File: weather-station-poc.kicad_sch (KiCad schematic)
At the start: 14 parts

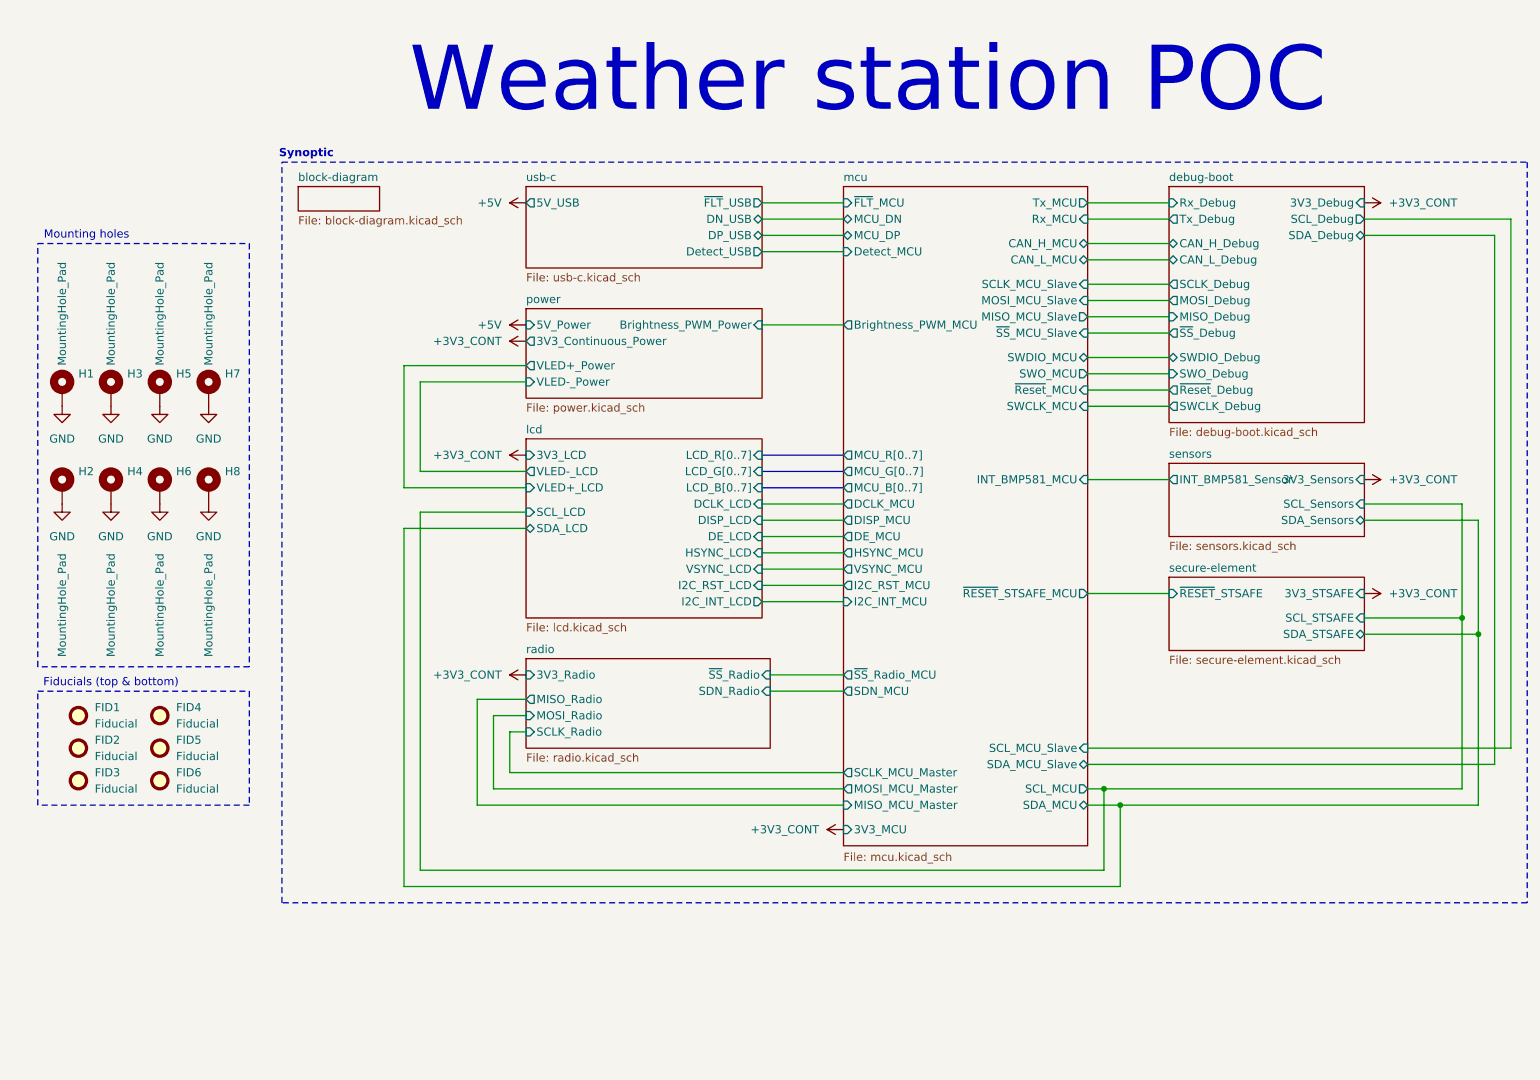
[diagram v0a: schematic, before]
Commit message: Rename main 3V3 label name
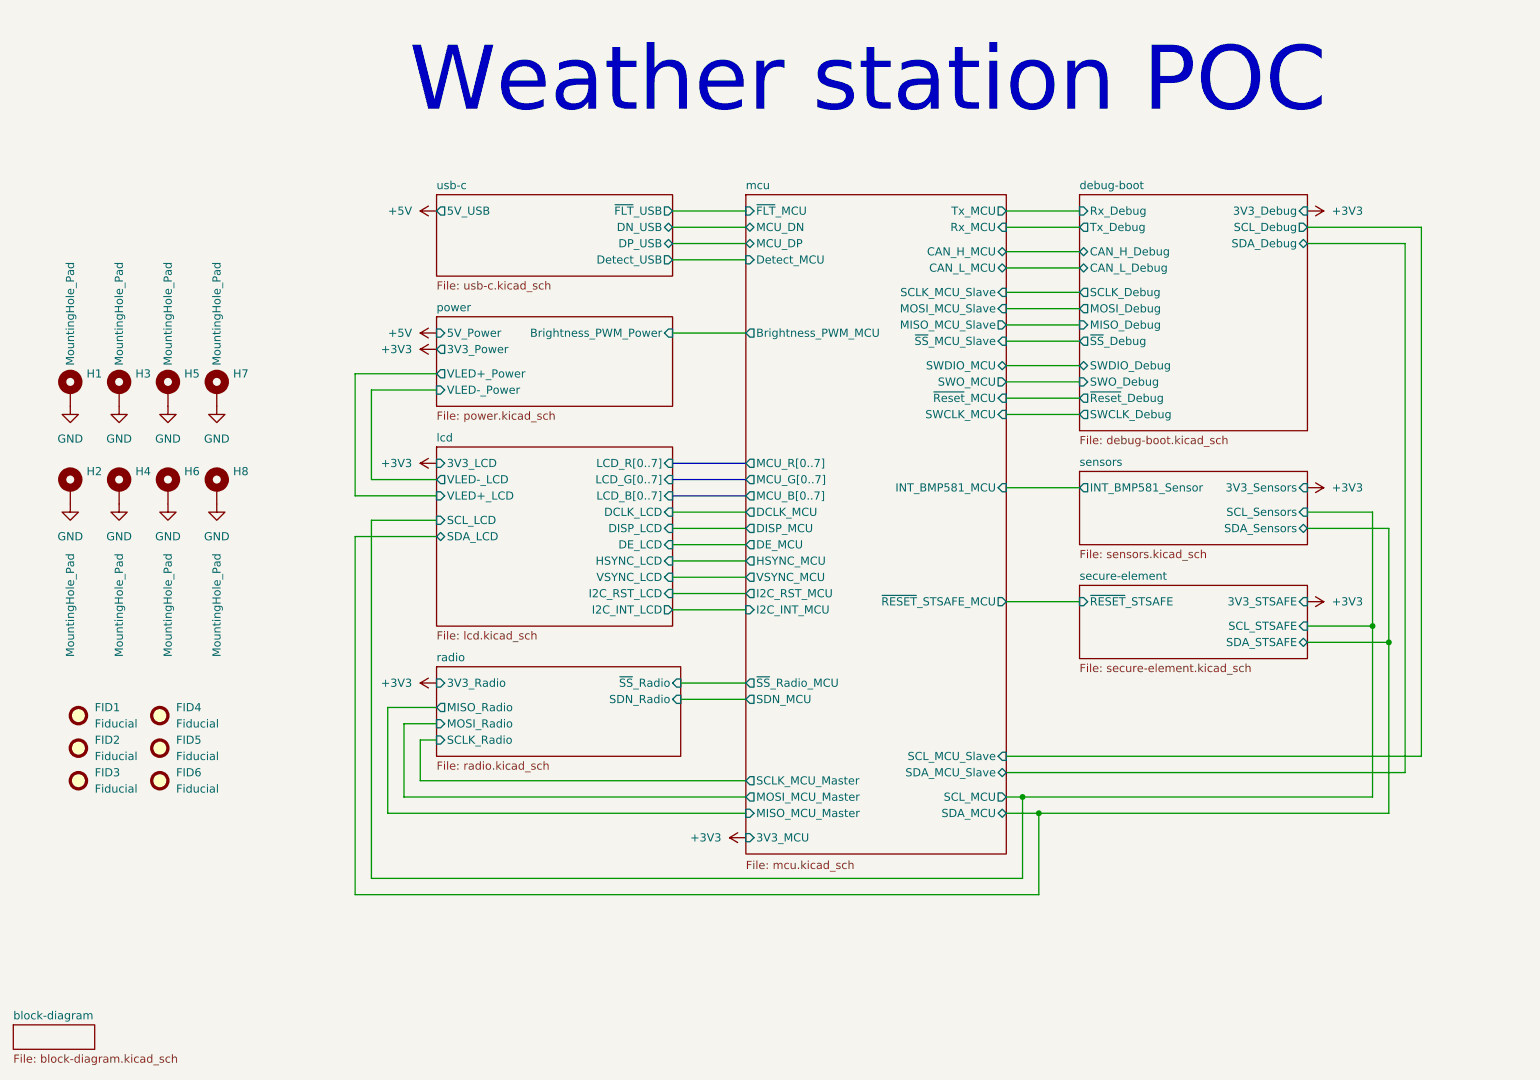
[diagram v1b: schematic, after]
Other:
- sheet power ports: added 3V3_Power; removed 3V3_Continuous_Power
- note removed: "Fiducials (top & bottom)"
- note removed: "Mounting holes"
- note removed: "Synoptic"
- moved on the sheet: H1, H2, H3, H4, H5, H6, H7, H8

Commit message: Move SWD debug connector from debug sheet to MCU sheet
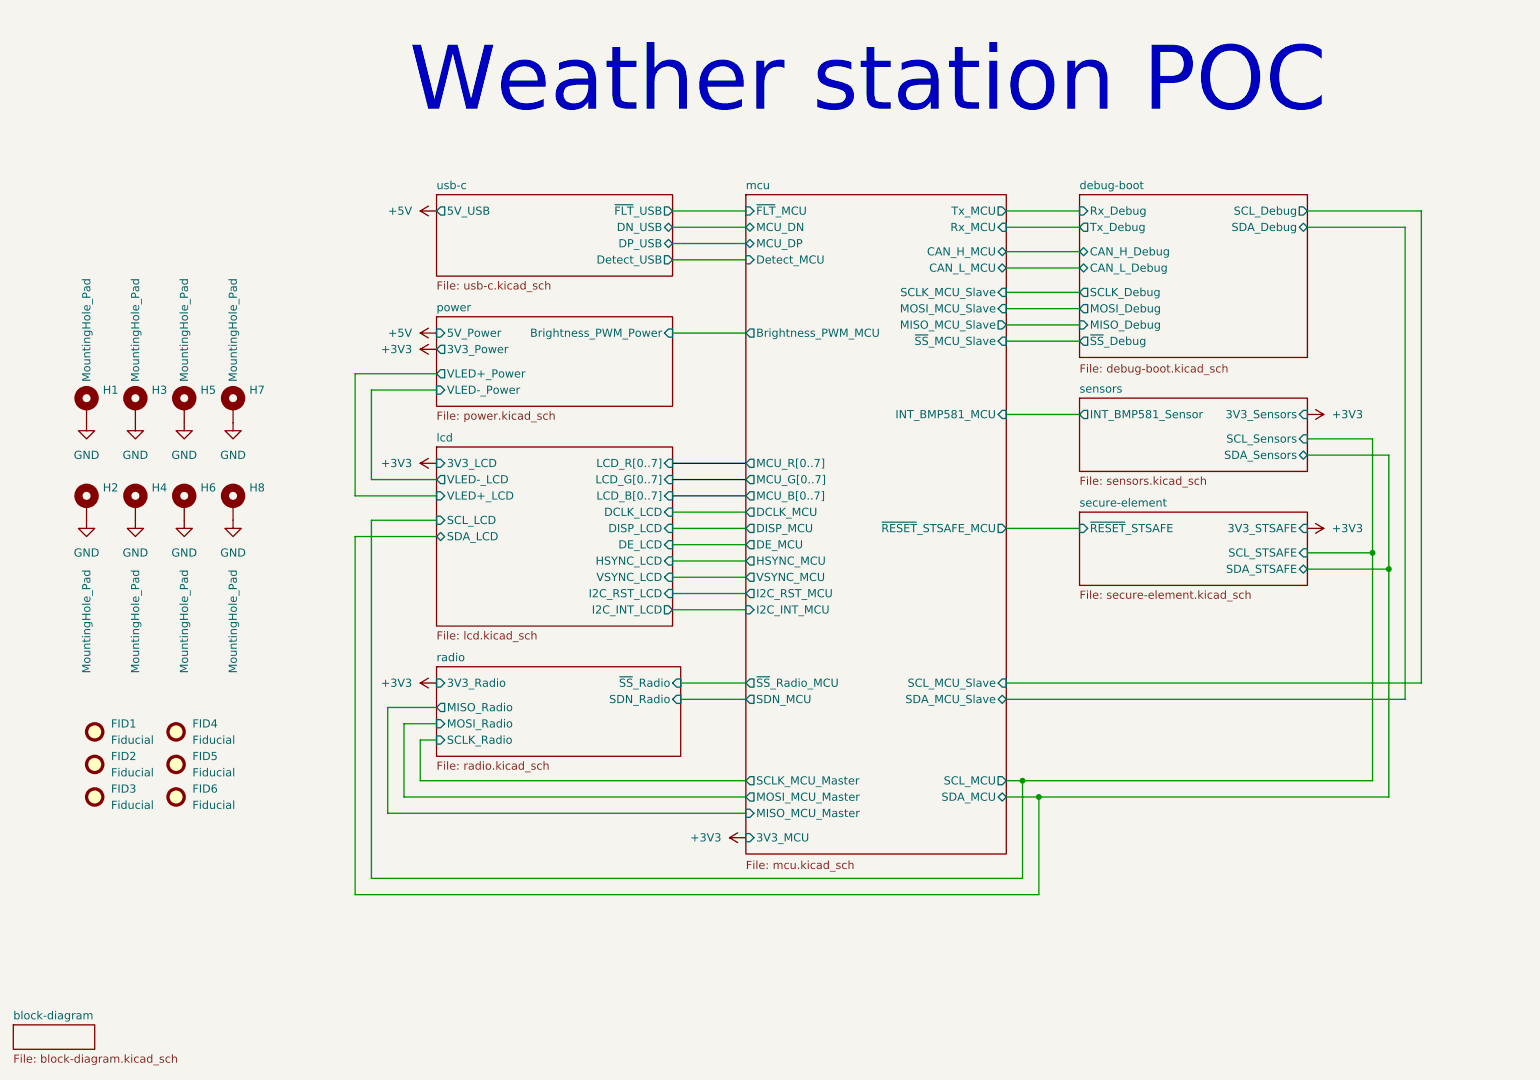
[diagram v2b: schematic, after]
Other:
- sheet debug-boot ports: added none; removed 3V3_Debug, SWCLK_Debug, SWDIO_Debug, SWO_Debug, ~{Reset}_Debug
- sheet mcu ports: added none; removed SWCLK_MCU, SWDIO_MCU, SWO_MCU, ~{Reset}_MCU
- moved on the sheet: FID1, FID2, FID3, FID4, FID5, FID6, H1, H2, H3, H4, H5, H6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

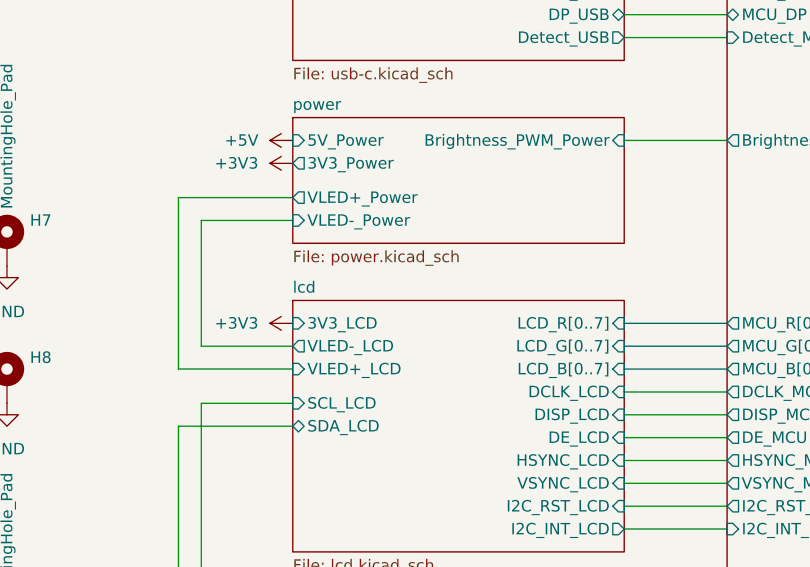
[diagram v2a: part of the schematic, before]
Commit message: Rename backlight power pins
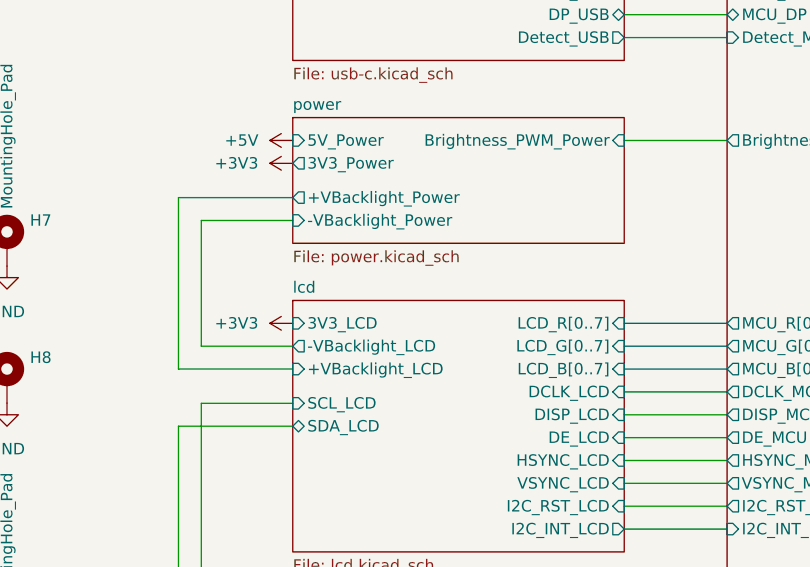
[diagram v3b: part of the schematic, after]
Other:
- sheet lcd ports: added +VBacklight_LCD, -VBacklight_LCD; removed VLED+_LCD, VLED-_LCD
- sheet power ports: added +VBacklight_Power, -VBacklight_Power; removed VLED+_Power, VLED-_Power
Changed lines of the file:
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@@
-			)
-		)
-		(pin "VLED+_Power" output
-			(at 81.28 68.58 180)
-			(effects
-				(font
-					(size 1.27 1.27)
-				)
-				(justify left)
-			)
-		)
-		(pin "VLED-_Power" input
-			(at 81.28 71.12 180)
-			(effects
-				(font
-					(size 1.27 1.27)
-				)
-				(justify left)
 			)
 		)
@@
 		(pin "3V3_Power" output
 			(at 81.28 64.77 180)
+			(effects
+				(font
+					(size 1.27 1.27)
+				)
+				(justify left)
+			)
+		)
+		(pin "+VBacklight_Power" output
+			(at 81.28 68.58 180)
+			(effects
+				(font
+					(size 1.27 1.27)
+				)
+				(justify left)
+			)
+		)
+		(pin "-VBacklight_Power" input
+			(at 81.28 71.12 180)
 			(effects
 				(font
@@
 			)
 		)
-		(pin "VLED+_LCD" input
-			(at 81.28 87.63 180)
-			(effects
-				(font
-					(size 1.27 1.27)
-				)
-				(justify left)
-			)
-		)
-		(pin "VLED-_LCD" output
-			(at 81.28 85.09 180)
-			(effects
-				(font
-					(size 1.27 1.27)
-				)
-				(justify left)
-			)
-		)
 		(pin "DCLK_LCD" input
 			(at 118.11 90.17 0)
@@
 			(effects
 				(font
+					(size 1.27 1.27)
+				)
+				(justify left)
+			)
+		)
+		(pin "+VBacklight_LCD" input
+			(at 81.28 87.63 180)
+			(effects
+				(font
+					(size 1.27 1.27)
+				)
+				(justify left)
+			)
+		)
+		(pin "-VBacklight_LCD" output
+			(at 81.28 85.09 180)
+			(effects
+				(font
